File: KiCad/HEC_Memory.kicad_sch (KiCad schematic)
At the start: 10 parts, among them U13 74LS245, U14 74LS245, U15 74LS32, U16 74LS32, U2 AS6C4008-55PCN, U22 74LS02, U3 AS6C4008-55PCN, U4 CY7C199, U5 CY7C199, U9 74LS574

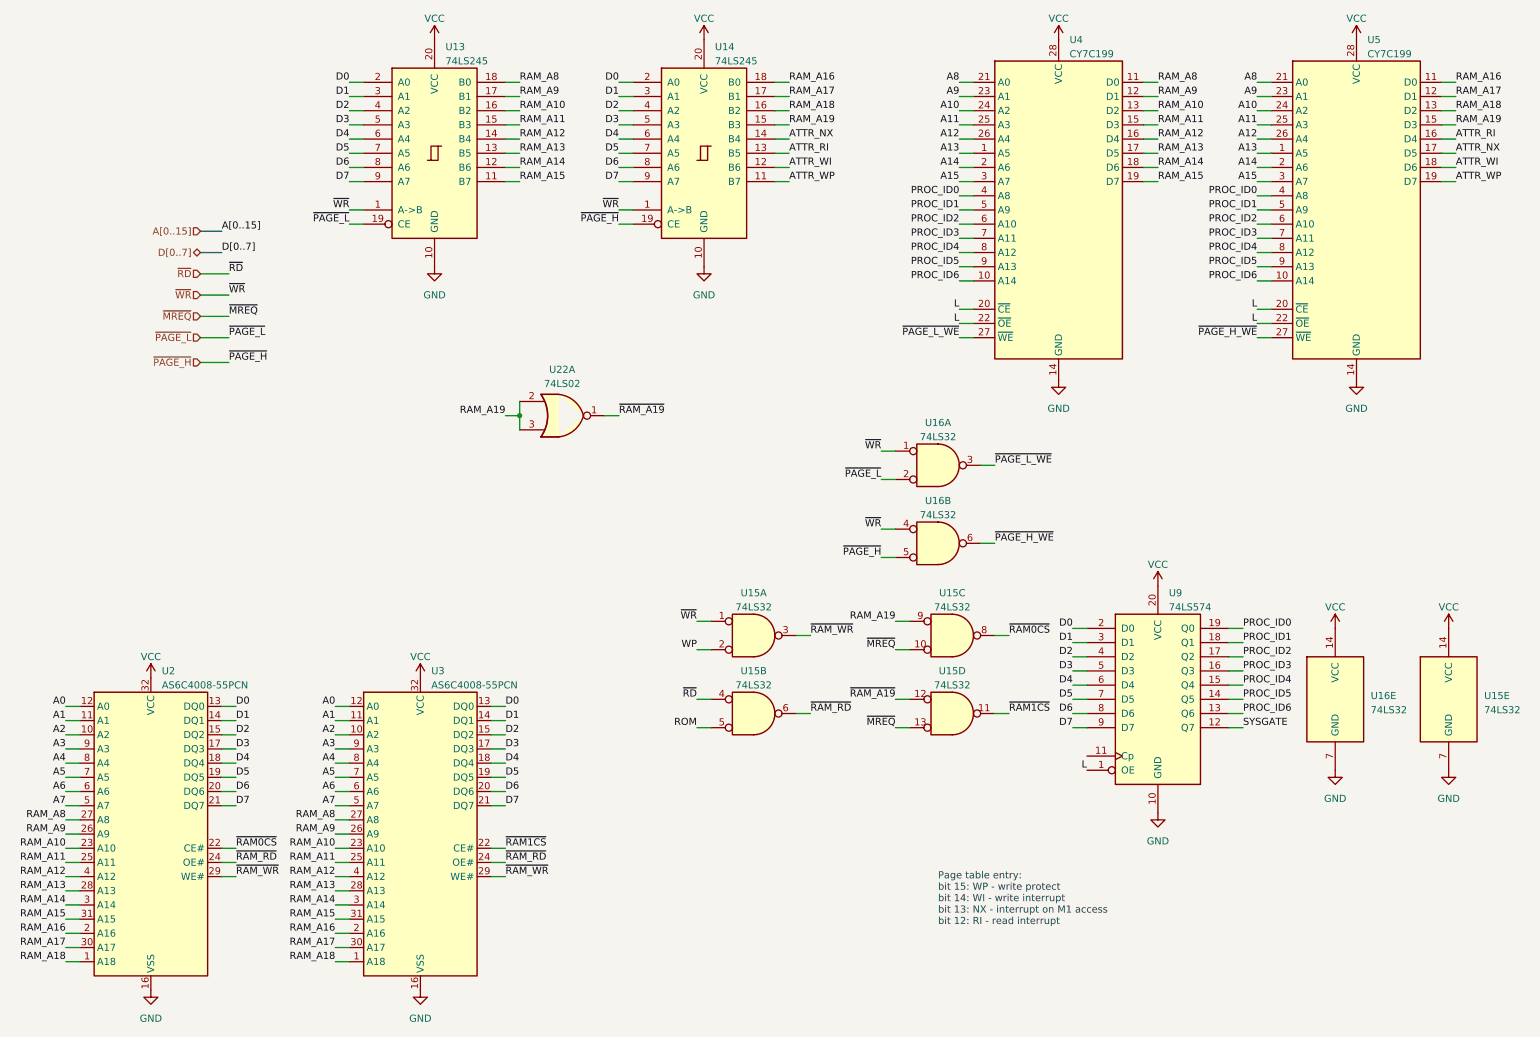
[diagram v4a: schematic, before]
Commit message: PCB Update
Some part placement, some routing, some change in schematic for easier PCB routing.
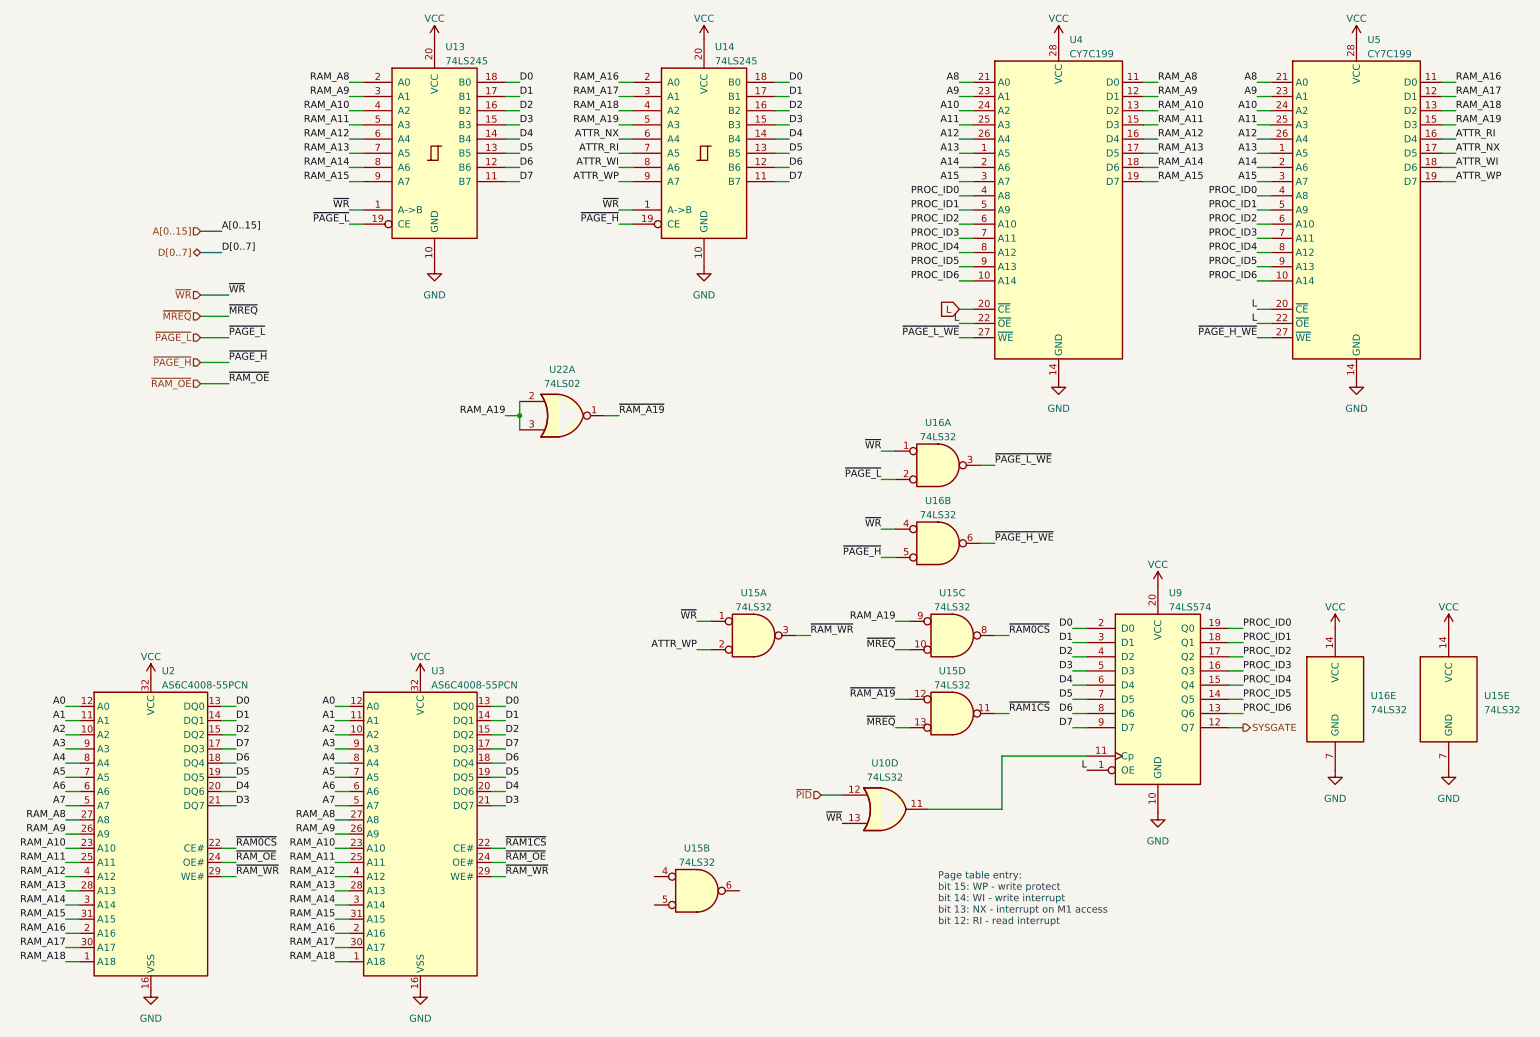
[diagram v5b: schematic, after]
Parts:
- added U10: 74LS32, symbol 74xx:74LS32
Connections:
- net WP is gone; now on net ATTR_WP: U15.2
- net ATTR_NX: now also U14.6 (A4); no longer U14.14 (B4)
- net ATTR_RI: now also U14.7 (A5); no longer U14.13 (B5)
- net ATTR_WI: now also U14.8 (A6); no longer U14.12 (B6)
- net ATTR_WP: now also U14.9 (A7); no longer U14.11 (B7)
- net D0: now also U13.18 (B0), U14.18 (B0); no longer U13.2 (A0), U14.2 (A0)
- net D1: now also U13.17 (B1), U14.17 (B1); no longer U13.3 (A1), U14.3 (A1)
- net D2: now also U13.16 (B2), U14.16 (B2); no longer U13.4 (A2), U14.4 (A2)
- net D3: now also U13.15 (B3), U14.15 (B3), U2.21 (DQ7), U3.21 (DQ7); no longer U13.5 (A3), U14.5 (A3), U2.17 (DQ3), U3.17 (DQ3)
- net D4: now also U13.14 (B4), U14.14 (B4), U2.20 (DQ6), U3.20 (DQ6); no longer U13.6 (A4), U14.6 (A4), U2.18 (DQ4), U3.18 (DQ4)
- net D5: now also U13.13 (B5), U14.13 (B5); no longer U13.7 (A5), U14.7 (A5)
- net D6: now also U13.12 (B6), U14.12 (B6), U2.18 (DQ4), U3.18 (DQ4); no longer U13.8 (A6), U14.8 (A6), U2.20 (DQ6), U3.20 (DQ6)
- net D7: now also U13.11 (B7), U14.11 (B7), U2.17 (DQ3), U3.17 (DQ3); no longer U13.9 (A7), U14.9 (A7), U2.21 (DQ7), U3.21 (DQ7)
- net RAM_A10: now also U13.4 (A2); no longer U13.16 (B2)
- net RAM_A11: now also U13.5 (A3); no longer U13.15 (B3)
- net RAM_A12: now also U13.6 (A4); no longer U13.14 (B4)
- net RAM_A13: now also U13.7 (A5); no longer U13.13 (B5)
- net RAM_A14: now also U13.8 (A6); no longer U13.12 (B6)
- net RAM_A15: now also U13.9 (A7); no longer U13.11 (B7)
- net RAM_A16: now also U14.2 (A0); no longer U14.18 (B0)
- net RAM_A17: now also U14.3 (A1); no longer U14.17 (B1)
- net RAM_A18: now also U14.4 (A2); no longer U14.16 (B2)
- net RAM_A19: now also U14.5 (A3); no longer U14.15 (B3)
- net RAM_A8: now also U13.2 (A0); no longer U13.18 (B0)
- net RAM_A9: now also U13.3 (A1); no longer U13.17 (B1)
- net ~{WR}: now also U10.13
- net at U9.11 (Cp): now also U10.11
- net ROM: no longer names the net of U15.5
- net ~{RAM_RD} renamed ~{RAM_OE}
- net ~{RAM_OE}: no longer U15.6
- net ~{RD}: no longer names the net of U15.4
- new net ~{PID}: U10.12
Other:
- moved on the sheet: U15B

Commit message: Add POST code circuit
Add circuit to show POST code using I register on Z80 to assist debugging.
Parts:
- U10: footprint (none) -> Package_DIP:DIP-14_W7.62mm_Socket
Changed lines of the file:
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@@
       (effects (font (size 1.27 1.27)))
     )
-    (property "Footprint" "" (at 169.545 158.115 0)
+    (property "Footprint" "Package_DIP:DIP-14_W7.62mm_Socket" (at 169.545 158.115 0)
       (effects (font (size 1.27 1.27)) hide)
     )

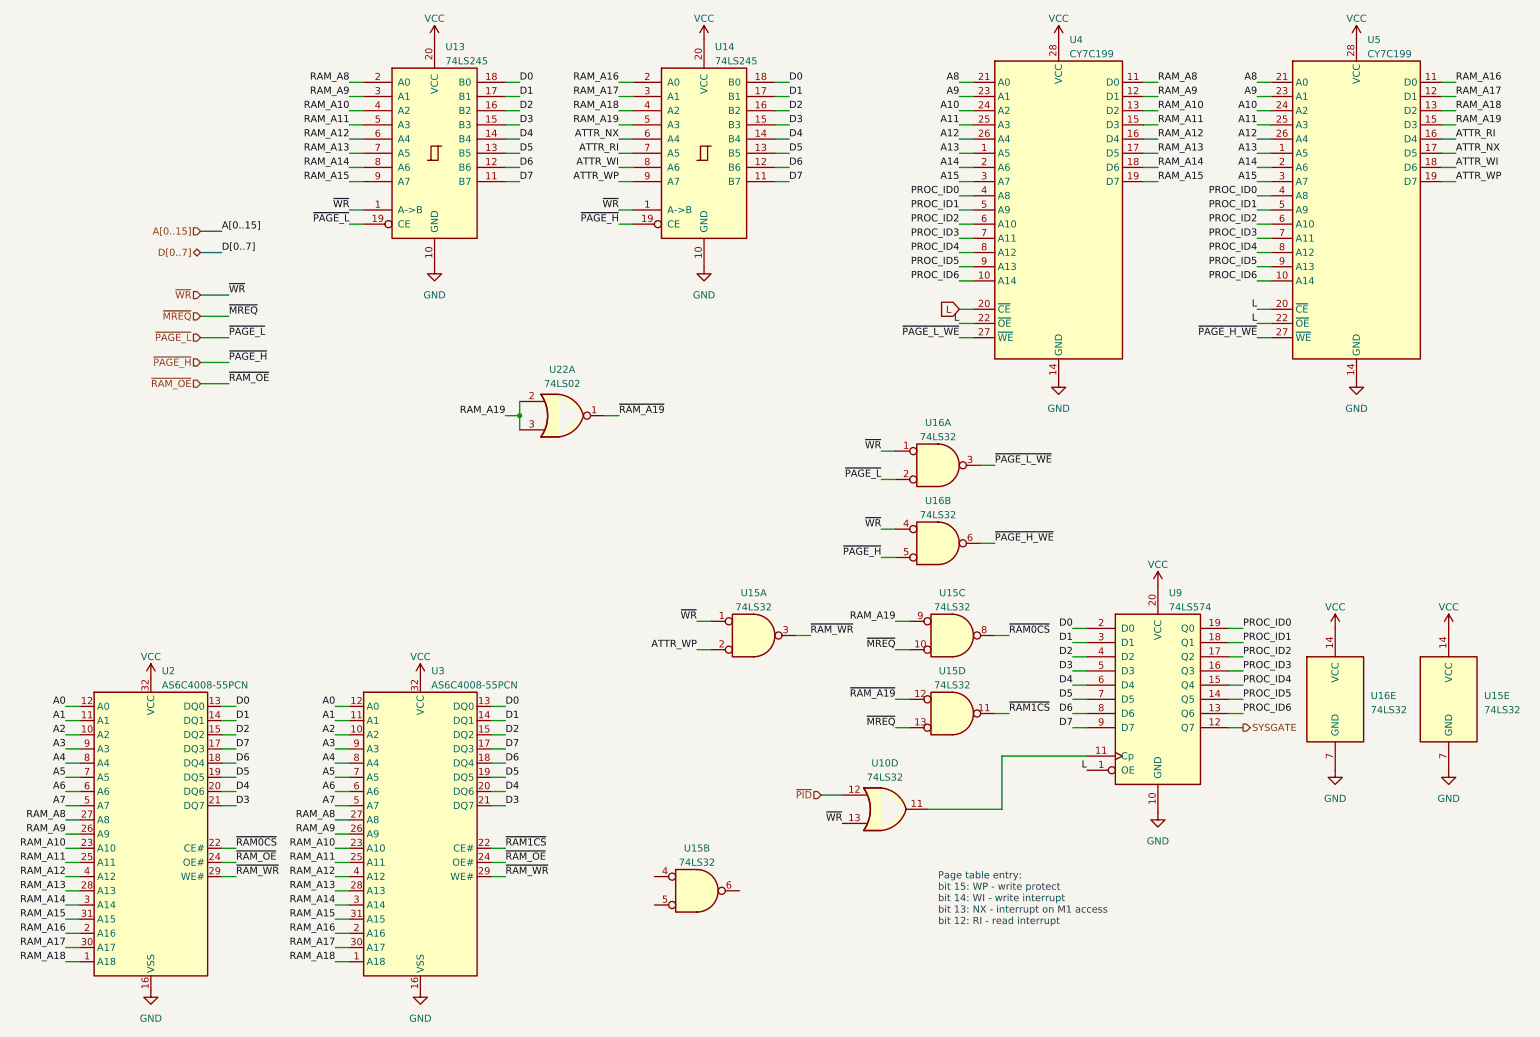
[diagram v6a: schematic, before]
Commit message: Cleanup schematic
Cleanup the schematic for easier reading, reduce ERC errors.
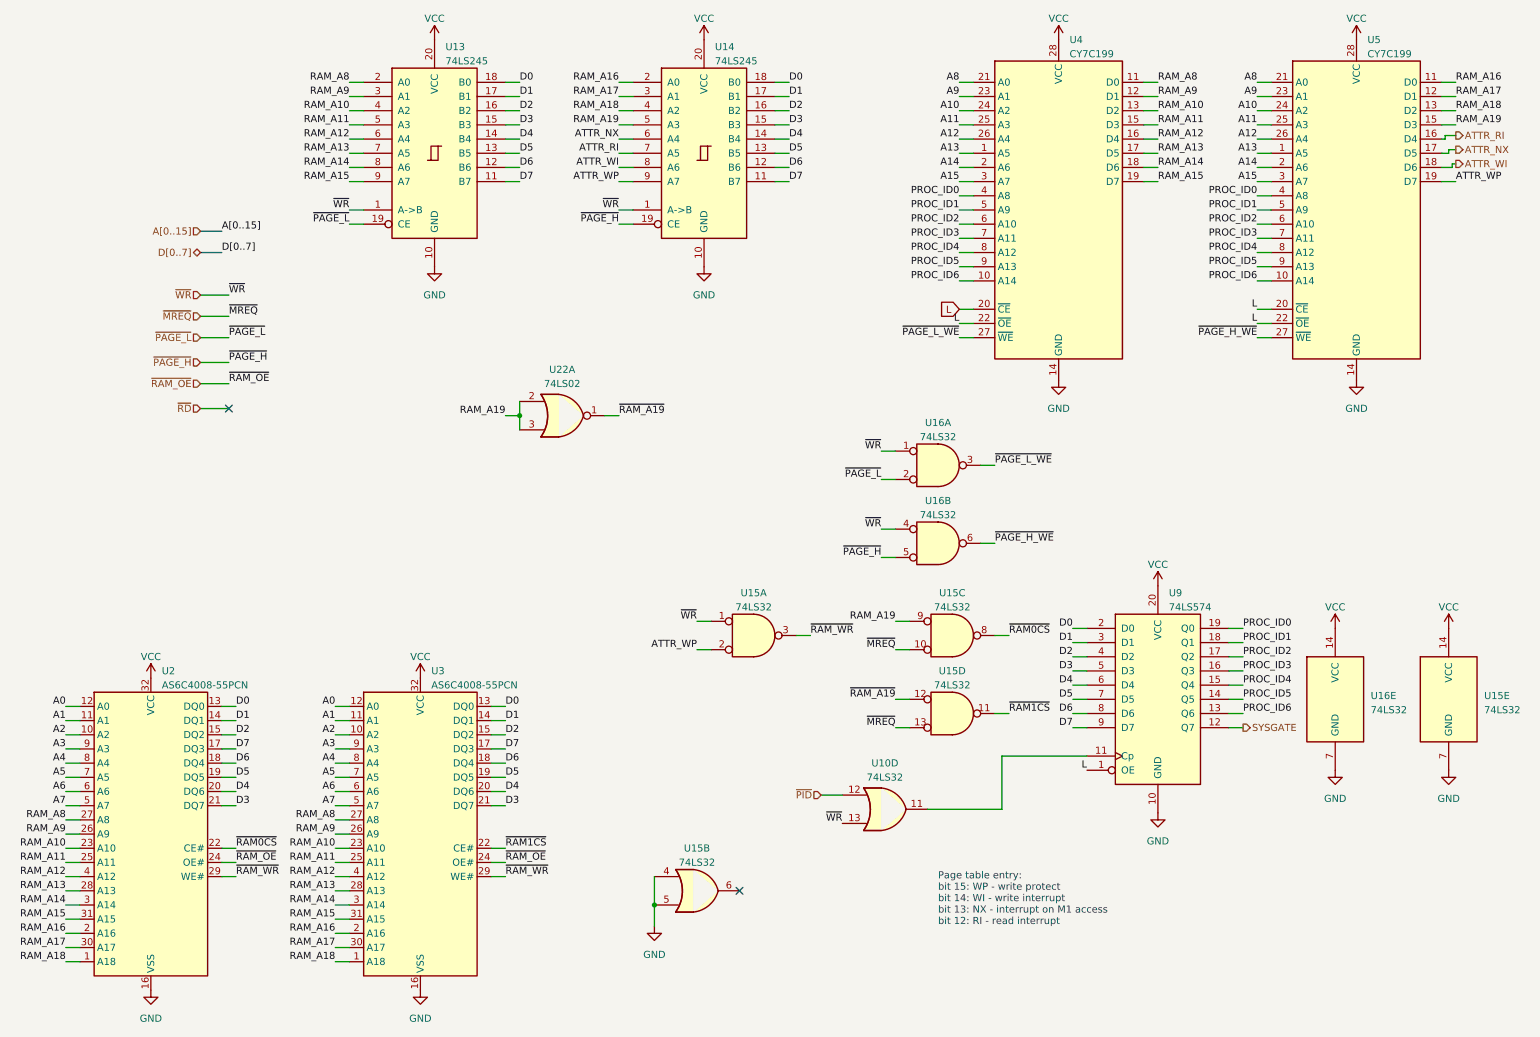
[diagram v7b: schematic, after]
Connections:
- net GND: now also U15.4, U15.5
- no-connect marks 0 -> 2
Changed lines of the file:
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@@
 (kicad_sch (version 20230121) (generator eeschema)
   (paper "A4")
+  (junction (at 128.27 175.26) (diameter 0) (color 0 0 0 0)
+  )
   (junction (at 104.14 87.63) (diameter 0) (color 0 0 0 0)
   )
+  (no_connect (at 52.07 86.36))
+  (no_connect (at 143.51 172.72))
   (wire (pts (xy 269.24 45.72) (xy 271.78 45.72))
     (stroke (width 0) (type default))
@@
     (stroke (width 0) (type default))
   )
-  (wire (pts (xy 269.24 43.18) (xy 271.78 43.18))
+  (wire (pts (xy 271.145 42.545) (xy 271.78 42.545))
     (stroke (width 0) (type default))
   )
@@
     (stroke (width 0) (type default))
   )
+  (wire (pts (xy 271.145 42.545) (xy 271.145 43.18))
+    (stroke (width 0) (type default))
+  )
   (wire (pts (xy 99.06 154.94) (xy 101.6 154.94))
     (stroke (width 0) (type default))
@@
     (stroke (width 0) (type default))
   )
+  (wire (pts (xy 269.875 38.1) (xy 269.24 38.1))
+    (stroke (width 0) (type default))
+  )
   (wire (pts (xy 22.86 175.26) (xy 25.4 175.26))
     (stroke (width 0) (type default))
@@
     (stroke (width 0) (type default))
   )
+  (wire (pts (xy 269.875 37.465) (xy 269.875 38.1))
+    (stroke (width 0) (type default))
+  )
   (wire (pts (xy 73.66 38.1) (xy 76.2 38.1))
     (stroke (width 0) (type default))
@@
     (stroke (width 0) (type default))
   )
-  (wire (pts (xy 269.24 38.1) (xy 271.78 38.1))
+  (wire (pts (xy 269.875 37.465) (xy 271.78 37.465))
     (stroke (width 0) (type default))
   )
@@
     (stroke (width 0) (type default))
   )
+  (wire (pts (xy 46.99 86.36) (xy 52.07 86.36))
+    (stroke (width 0) (type default))
+  )
   (wire (pts (xy 22.86 157.48) (xy 25.4 157.48))
     (stroke (width 0) (type default))
@@
     (stroke (width 0) (type default))
   )
+  (wire (pts (xy 128.27 170.18) (xy 128.27 175.26))
+    (stroke (width 0) (type default))
+  )
   (wire (pts (xy 22.86 167.64) (xy 25.4 167.64))
     (stroke (width 0) (type default))
@@
     (stroke (width 0) (type default))
   )
+  (wire (pts (xy 271.145 43.18) (xy 269.24 43.18))
+    (stroke (width 0) (type default))
+  )
   (wire (pts (xy 71.12 167.64) (xy 73.66 167.64))
     (stroke (width 0) (type default))
@@
     (stroke (width 0) (type default))
   )
-  (wire (pts (xy 269.24 40.64) (xy 271.78 40.64))
+  (wire (pts (xy 270.51 40.005) (xy 271.78 40.005))
     (stroke (width 0) (type default))
   )
@@
     (stroke (width 0) (type default))
   )
+  (wire (pts (xy 128.27 175.26) (xy 128.27 179.07))
+    (stroke (width 0) (type default))
+  )
   (wire (pts (xy 99.06 152.4) (xy 101.6 152.4))
     (stroke (width 0) (type default))
@@
     (stroke (width 0) (type default))
   )
+  (wire (pts (xy 270.51 40.64) (xy 269.24 40.64))
+    (stroke (width 0) (type default))
+  )
   (wire (pts (xy 46.99 81.915) (xy 52.07 81.915))
     (stroke (width 0) (type default))
@@
   )
   (wire (pts (xy 149.86 45.72) (xy 152.4 45.72))
+    (stroke (width 0) (type default))
+  )
+  (wire (pts (xy 270.51 40.005) (xy 270.51 40.64))
     (stroke (width 0) (type default))
   )
@@
     (effects (font (size 1.27 1.27)) (justify right bottom))
   )
-  (label "ATTR_NX" (at 271.78 40.64 0) (fields_autoplaced)
-    (effects (font (size 1.27 1.27)) (justify left bottom))
-  )
   (label "PROC_ID6" (at 182.88 63.5 180) (fields_autoplaced)
     (effects (font (size 1.27 1.27)) (justify right bottom))
@@
     (effects (font (size 1.27 1.27)) (justify right bottom))
   )
-  (label "ATTR_RI" (at 271.78 38.1 0) (fields_autoplaced)
-    (effects (font (size 1.27 1.27)) (justify left bottom))
-  )
   (label "RAM_A15" (at 73.66 45.72 180) (fields_autoplaced)
     (effects (font (size 1.27 1.27)) (justify right bottom))
@@
   (label "RAM_A17" (at 22.86 182.88 180) (fields_autoplaced)
     (effects (font (size 1.27 1.27)) (justify right bottom))
-  )
-  (label "ATTR_WI" (at 271.78 43.18 0) (fields_autoplaced)
-    (effects (font (size 1.27 1.27)) (justify left bottom))
   )
   (label "RAM_A15" (at 71.12 177.8 180) (fields_autoplaced)
@@
     )
   )
+  (hierarchical_label "ATTR_WI" (shape output) (at 271.78 42.545 0) (fields_autoplaced)
+    (effects (font (size 1.27 1.27)) (justify left))
+  )
   (hierarchical_label "~{PAGE_L}" (shape input) (at 46.99 73.66 180) (fields_autoplaced)
     (effects (font (size 1.27 1.27)) (justify right))
@@
     (effects (font (size 1.27 1.27)) (justify left))
   )
+  (hierarchical_label "ATTR_NX" (shape output) (at 271.78 40.005 0) (fields_autoplaced)
+    (effects (font (size 1.27 1.27)) (justify left))
+  )
   (hierarchical_label "~{MREQ}" (shape input) (at 46.99 69.85 180) (fields_autoplaced)
     (effects (font (size 1.27 1.27)) (justify right))
@@
     (effects (font (size 1.27 1.27)) (justify right))
   )
+  (hierarchical_label "ATTR_RI" (shape output) (at 271.78 37.465 0) (fields_autoplaced)
+    (effects (font (size 1.27 1.27)) (justify left))
+  )
   (hierarchical_label "~{RAM_OE}" (shape input) (at 46.99 81.915 180) (fields_autoplaced)
     (effects (font (size 1.27 1.27)) (justify right))
@@
     (effects (font (size 1.27 1.27)) (justify right))
   )
+  (hierarchical_label "~{RD}" (shape input) (at 46.99 86.36 180) (fields_autoplaced)
+    (effects (font (size 1.27 1.27)) (justify right))
+  )
   (symbol (lib_id "power:VCC") (at 270.51 125.73 0) (unit 1)
     (in_bom yes) (on_board yes) (dnp no) (fields_autoplaced)
@@
         (path "/87935374-b60a-4f41-99da-94b76103dd77/933a6f90-eb98-4eb1-8c19-8a76228aece1"
           (reference "#PWR011") (unit 1)
+        )
+      )
+    )
+  )
+  (symbol (lib_id "power:GND") (at 128.27 179.07 0) (unit 1)
+    (in_bom yes) (on_board yes) (dnp no) (fields_autoplaced)
+    (property "Reference" "#PWR0108" (at 128.27 185.42 0)
+      (effects (font (size 1.27 1.27)) hide)
+    )
+    (property "Value" "GND" (at 128.27 184.15 0)
+      (effects (font (size 1.27 1.27)))
+    )
+    (property "Footprint" "" (at 128.27 179.07 0)
+      (effects (font (size 1.27 1.27)) hide)
+    )
+    (property "Datasheet" "" (at 128.27 179.07 0)
+      (effects (font (size 1.27 1.27)) hide)
+    )
+    (pin "1")
+    (instances
+      (project "HEC1"
+        (path "/87935374-b60a-4f41-99da-94b76103dd77"
+          (reference "#PWR0108") (unit 1)
+        )
+        (path "/87935374-b60a-4f41-99da-94b76103dd77/933a6f90-eb98-4eb1-8c19-8a76228aece1"
+          (reference "#PWR0109") (unit 1)
         )
       )
@@
     )
   )
-  (symbol (lib_id "74xx:74LS32") (at 135.89 172.72 0) (unit 2) (convert 2)
+  (symbol (lib_id "74xx:74LS32") (at 135.89 172.72 0) (unit 2)
     (in_bom yes) (on_board yes) (dnp no) (fields_autoplaced)
     (property "Reference" "U15" (at 135.89 165.1 0)
